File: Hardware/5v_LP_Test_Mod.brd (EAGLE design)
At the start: 15.2 x 8.6 mm, 7 parts, among them J1 CONN_3, U1 TLV61220DBV

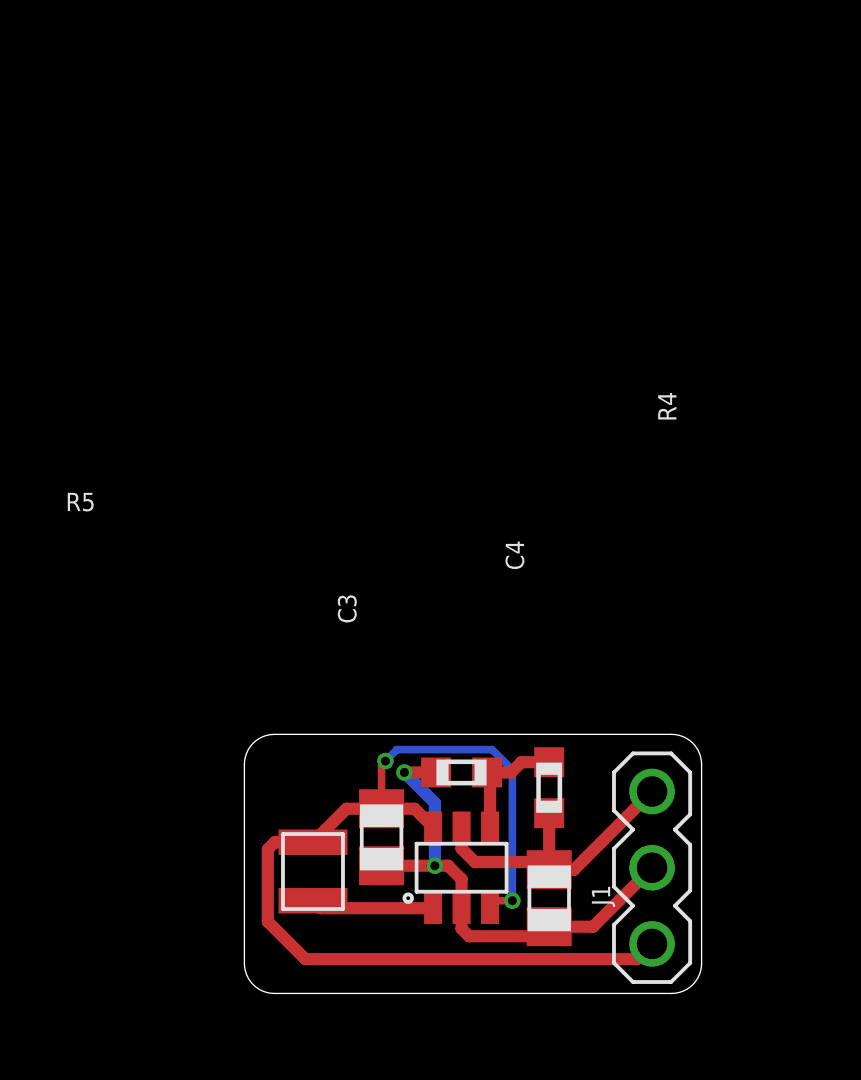
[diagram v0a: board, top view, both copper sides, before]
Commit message: Updated test boards for VolteraV1
Attempted to maximize compatibility with Voltera V1 system
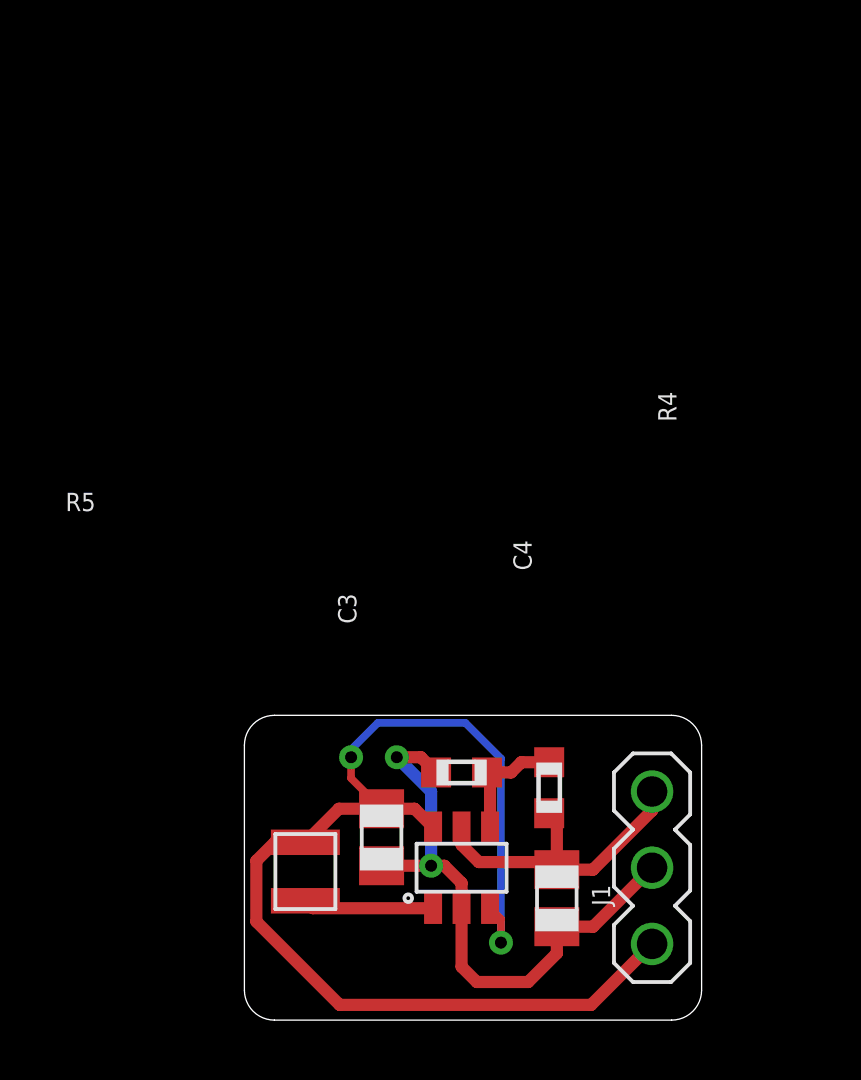
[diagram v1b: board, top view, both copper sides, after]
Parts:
- moved L1 0.25 mm to (2.03, 4.06)
- moved C4 0.25 mm to (10.4, 3.17)
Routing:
- net VIN: track 33.8 -> 39.8 mm
- net GND: track 16.5 -> 20.0 mm
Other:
- board size 15.2 x 8.6 mm -> 15.2 x 10.2 mm

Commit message: Updates to 5v test board
Added additional converter to 5v test setup, also condensed all units onto a single board and generated gerbers for compatibility with Sunstone PCB
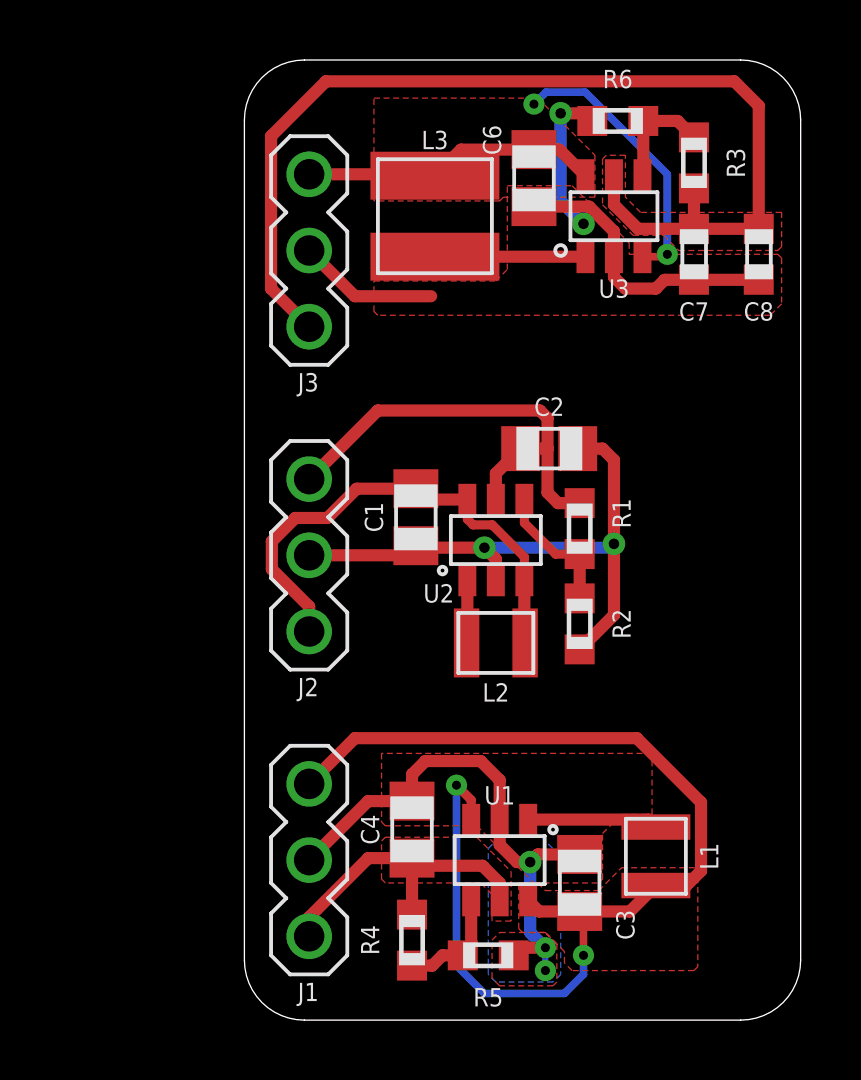
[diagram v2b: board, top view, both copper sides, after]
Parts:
- added C1, C2: 10uF, bschulz_passives:C0805
- added C6: (no value), bschulz_passives:C0805
- added C7, C8: (no value), bschulz_passives:C0603
- added J2, J3: CONN_3, bschulz:1X03
- added L2: 6.8uH, bschulz:1008
- added L3: (no value), bschulz:WE-TPC(3.8X3.8)
- added R1: 1.62M, bschulz_passives:R0603
- added R2: 180K, bschulz_passives:R0603
- added R3, R6: (no value), bschulz_passives:R0603
- added U2: TLV61220DBV, bschulz:DBV_R-PDSO-G6
- added U3: TPS61070DDC, bschulz:DDC_R-PDSO-G6
- moved L1 11.7 mm to (13.7, 4.57), turned to 90 degrees
- moved J1 11.4 mm to (2.16, 4.45), turned to 270 degrees
- moved R4 6.83 mm to (5.59, 1.78), turned to 90 degrees
- moved C3 6.78 mm to (11.2, 3.68), turned to 90 degrees
- moved R5 6.16 mm to (8.13, 1.27), turned to 180 degrees
- moved C4 5.34 mm to (5.59, 5.46), turned to 90 degrees
- moved U1 1.30 mm to (8.51, 4.45), turned to 180 degrees
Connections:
- new net GND1: C1.2, C2.2, J2.2, R2.1, U2.2
- new net GND2: C6.2, C7.2, C8.2, J3.2, R6.1, U3.2
- new net N$1: R1.1, R2.2, U2.4
- new net N$2: L3.2, U3.1
- new net N$5: L2.2, U2.1
- new net N$6: R3.1, R6.2, U3.4
- new net VIN1: C1.1, J2.3, L2.1, U2.3, U2.6
- new net VIN2: C6.1, J3.1, L3.1, U3.3, U3.6
- new net VOUT1: C2.1, J2.1, R1.2, U2.5
- new net VOUT2: C7.1, C8.1, J3.3, R3.2, U3.5
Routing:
- net VOUT2: track 0.00 -> 35.8 mm
- net GND1: track 0.00 -> 19.8 mm, vias 0 -> 2
- net GND2: track 0.00 -> 19.5 mm, vias 0 -> 2
- net VIN2: track 0.00 -> 19.3 mm, vias 0 -> 2
- net VIN1: track 0.00 -> 16.9 mm
- net VOUT1: track 0.00 -> 15.6 mm
- net N$2: track 0.00 -> 5.02 mm
- net N$1: track 0.00 -> 4.53 mm
- net N$6: track 0.00 -> 3.75 mm
- net N$5: track 0.00 -> 2.09 mm
- net VIN: track 39.8 -> 37.7 mm
- net GND: track 20.0 -> 18.7 mm, vias 2 -> 3
- added copper zone on layer 1, net GND
- added copper zone on layer 16, net GND
- added copper zone on layer 1, net GND2
- added copper zone on layer 1, net VIN
- added copper zone on layer 1, net VIN2
- added copper zone on layer 1, net VOUT
- added copper zone on layer 1, net VOUT2
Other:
- board size 15.2 x 10.2 mm -> 18.5 x 32 mm
- board text added: "Alternative"
- board text added: "Control"
- board text added: "GND"
- board text added: "Modified"
- board text added: "Vin"
- board text added: "Vout"
